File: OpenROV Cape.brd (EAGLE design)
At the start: 71.8 x 54.6 mm, 22 parts, among them IC1 ATMEGA328P-PU, T2 TIP122, T3 2N2222

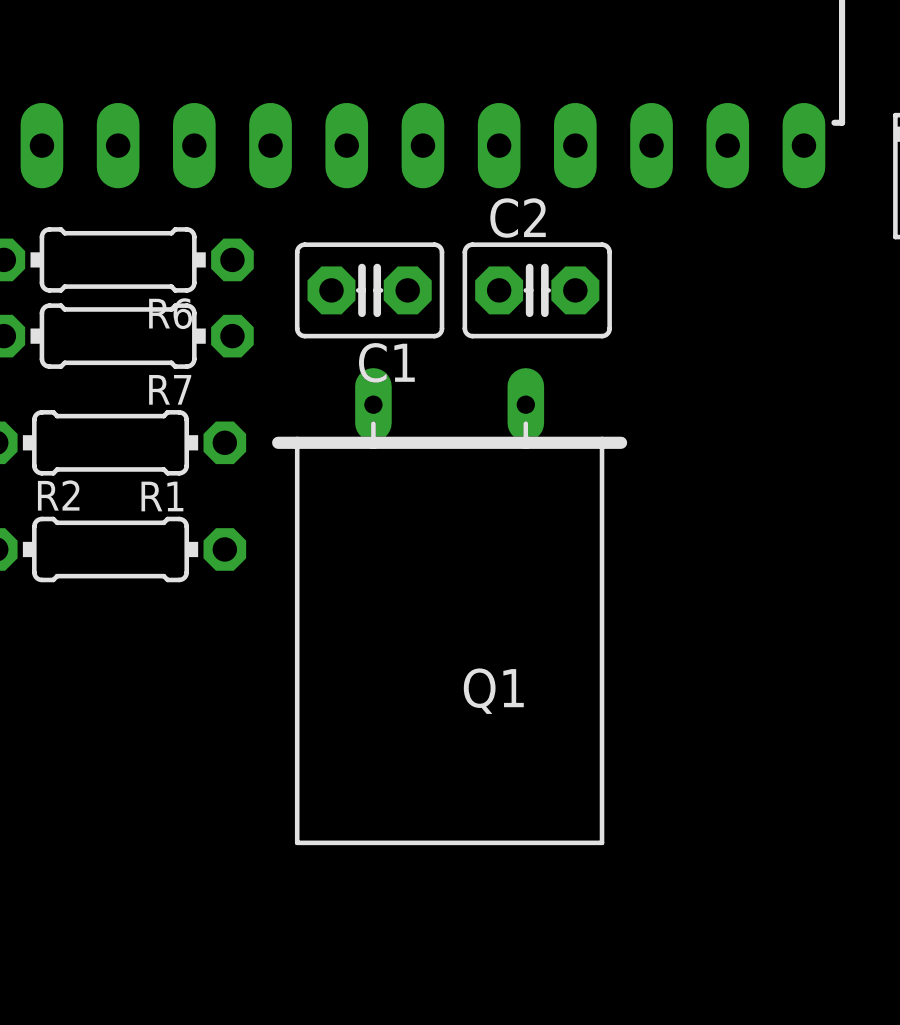
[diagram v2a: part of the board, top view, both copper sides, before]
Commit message: swapped out the giant crystal footprint for a smaller standard one with the same hole spacing
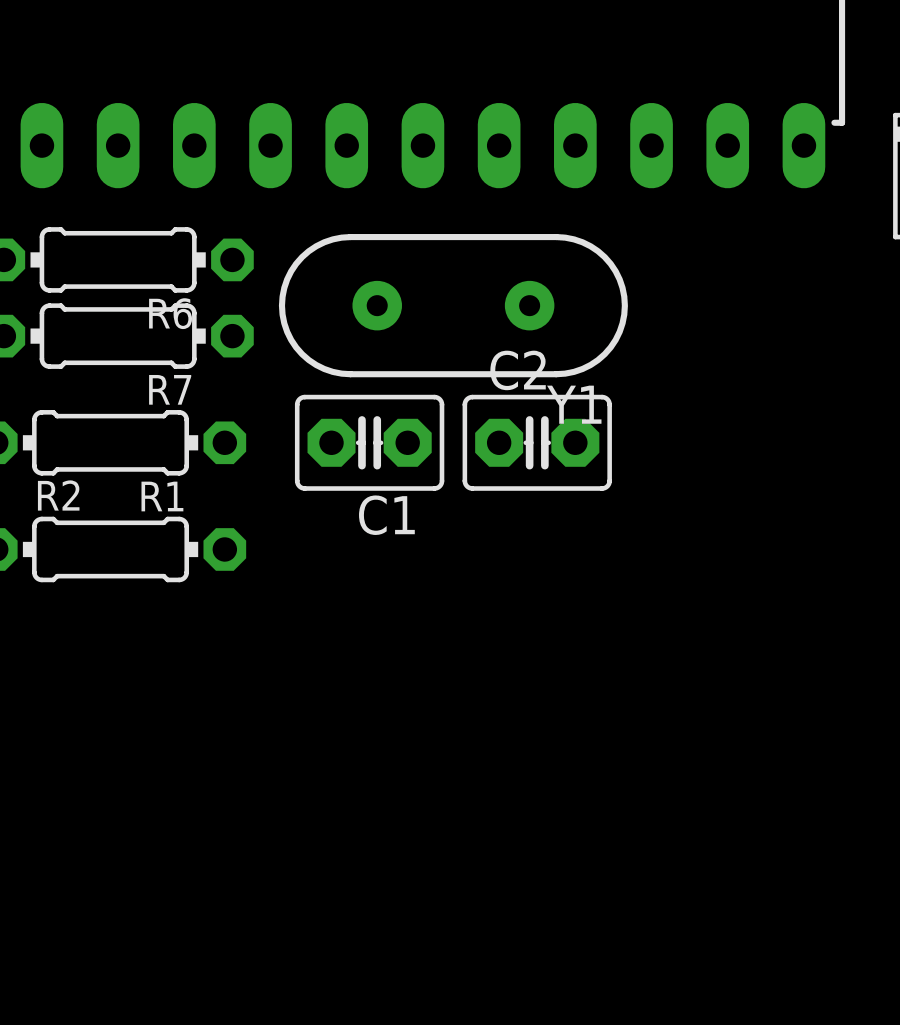
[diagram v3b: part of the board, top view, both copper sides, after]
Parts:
- removed Q1: (no value), special:Q
- added Y1: 16Mhz, SparkFun:HC49US
- moved C1 5.08 mm to (45.2, 25.7)
- moved C2 5.08 mm to (50.8, 25.7)
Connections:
- net N$24: now also Y1.1; no longer Q1.1
- net N$25: now also Y1.2; no longer Q1.2
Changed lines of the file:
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@@
 <element name="R1" library="rcl" package="0204/7" value="" x="36.576" y="25.654" rot="R180"/>
 <element name="R2" library="rcl" package="0204/7" value="" x="36.576" y="22.098"/>
-<element name="Q1" library="special" package="Q" value="" x="47.879" y="19.304" rot="R180"/>
-<element name="C1" library="capacitor-wima" package="C2.5-3" value="" x="45.212" y="30.734" rot="R180"/>
-<element name="C2" library="capacitor-wima" package="C2.5-3" value="" x="50.8" y="30.734"/>
+<element name="C1" library="capacitor-wima" package="C2.5-3" value="" x="45.212" y="25.654" rot="R180"/>
+<element name="C2" library="capacitor-wima" package="C2.5-3" value="" x="50.8" y="25.654"/>
 <element name="D1" library="diode" package="DO41-10" value="1N4004" x="66.548" y="34.544" rot="R270"/>
 <element name="D2" library="diode" package="DO41-10" value="1N4004" x="69.85" y="22.352" rot="R90"/>
@@
 <element name="T3" library="transistor" package="TO18" value="2N2222" x="29.21" y="27.94" rot="R90"/>
 <element name="R7" library="rcl" package="0204/7" value="" x="36.83" y="29.21" rot="R180"/>
+<element name="Y1" library="SparkFun" package="HC49US" value="16Mhz" x="48.006" y="30.226" rot="R180"/>
 </elements>
 <signals>
@@
 <contactref element="T3" pad="1"/>
 <wire x1="66.802" y1="23.368" x2="75.438" y2="24.892" width="0" layer="19" extent="1-1"/>
-<wire x1="52.07" y1="30.734" x2="66.802" y2="23.368" width="0" layer="19" extent="1-1"/>
+<wire x1="52.07" y1="25.654" x2="66.802" y2="23.368" width="0" layer="19" extent="1-1"/>
 <wire x1="72.39" y1="4.445" x2="66.802" y2="23.368" width="0" layer="19" extent="1-1"/>
-<wire x1="40.386" y1="25.654" x2="52.07" y2="30.734" width="0" layer="19" extent="1-1"/>
-<wire x1="43.942" y1="30.734" x2="40.386" y2="25.654" width="0" layer="19" extent="1-1"/>
+<wire x1="40.386" y1="25.654" x2="52.07" y2="25.654" width="0" layer="19" extent="1-1"/>
+<wire x1="43.942" y1="25.654" x2="40.386" y2="25.654" width="0" layer="19" extent="1-1"/>
 <wire x1="22.352" y1="19.558" x2="40.386" y2="25.654" width="0" layer="19" extent="1-1"/>
 <wire x1="22.352" y1="29.464" x2="22.352" y2="19.558" width="0" layer="19" extent="1-1"/>
@@
 </signal>
 <signal name="N$24">
-<contactref element="Q1" pad="1"/>
 <contactref element="C2" pad="1"/>
 <contactref element="IC1" pad="10"/>
-<wire x1="49.53" y1="30.734" x2="49.53" y2="35.56" width="0" layer="19" extent="1-1"/>
-<wire x1="50.419" y1="26.924" x2="49.53" y2="30.734" width="0" layer="19" extent="1-1"/>
+<contactref element="Y1" pad="1"/>
+<wire x1="49.53" y1="25.654" x2="49.53" y2="35.56" width="0" layer="19" extent="1-1"/>
+<wire x1="50.546" y1="30.226" x2="49.53" y2="25.654" width="0" layer="19" extent="1-1"/>
 </signal>
 <signal name="N$25">
-<contactref element="Q1" pad="2"/>
 <contactref element="C1" pad="1"/>
 <contactref element="IC1" pad="9"/>
-<wire x1="46.482" y1="30.734" x2="46.99" y2="35.56" width="0" layer="19" extent="1-1"/>
-<wire x1="45.339" y1="26.924" x2="46.482" y2="30.734" width="0" layer="19" extent="1-1"/>
+<contactref element="Y1" pad="2"/>
+<wire x1="46.482" y1="25.654" x2="46.99" y2="35.56" width="0" layer="19" extent="1-1"/>
+<wire x1="45.466" y1="30.226" x2="46.482" y2="25.654" width="0" layer="19" extent="1-1"/>
 </signal>
 <signal name="N$71">

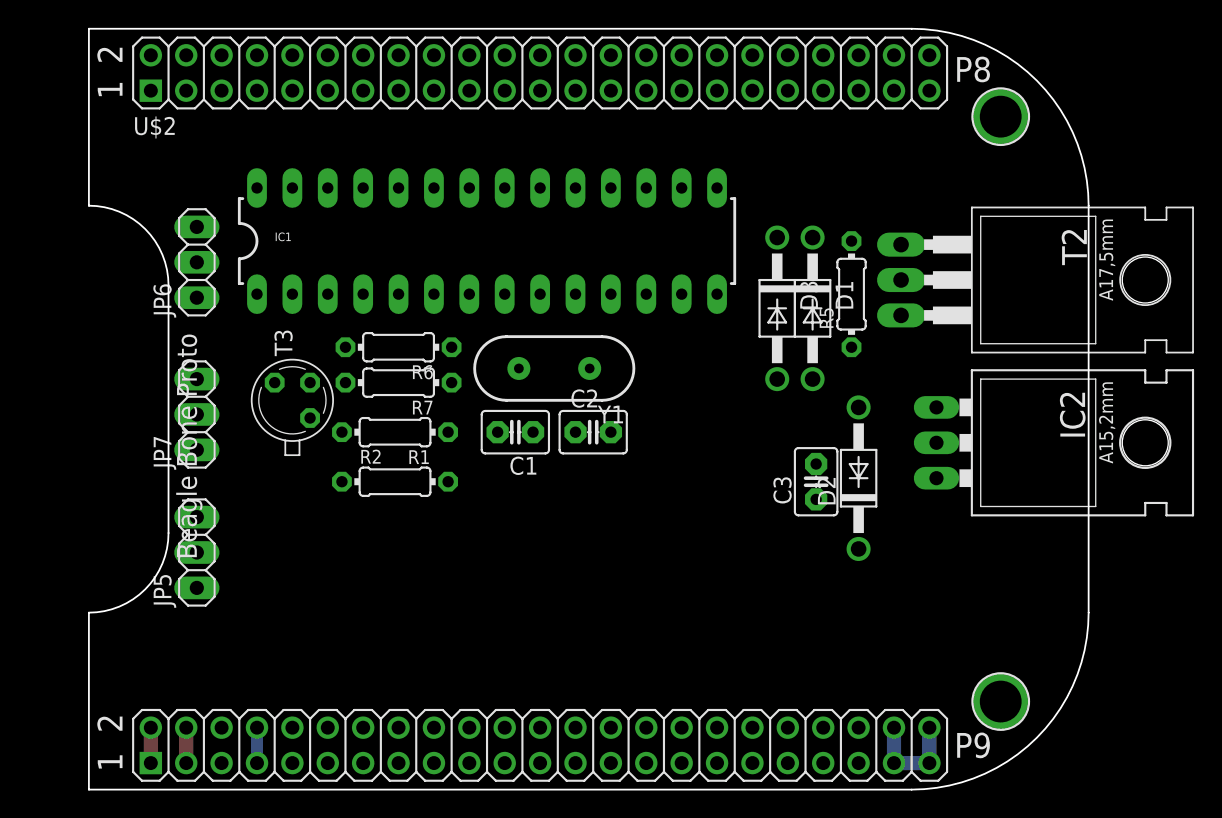
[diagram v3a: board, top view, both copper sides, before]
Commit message: moved servo headers back over to the right side of the board
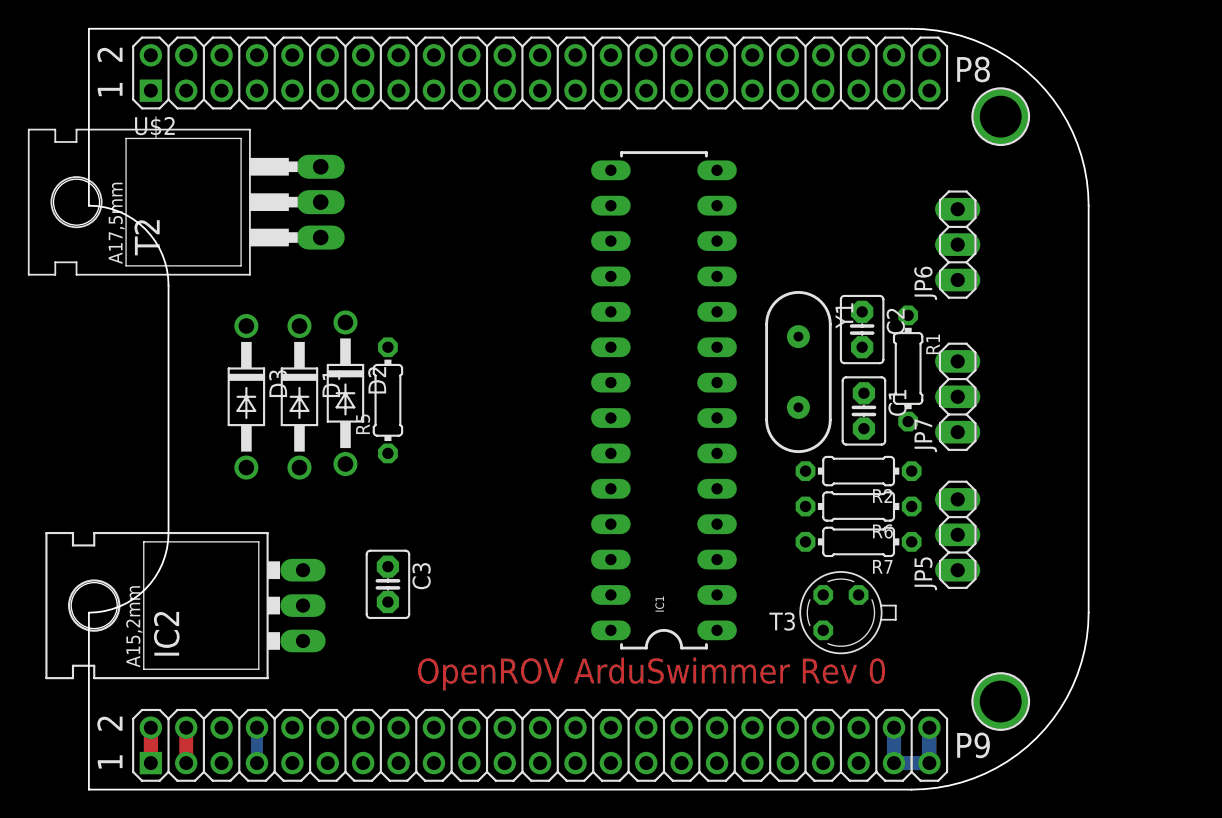
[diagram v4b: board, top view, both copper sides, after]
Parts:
- moved T2 54.6 mm to (24.9, 42.2), turned to 90 degrees
- moved JP5 54.6 mm to (77.0, 18.3)
- moved JP6 54.6 mm to (77.0, 39.1)
- moved JP7 54.6 mm to (77.0, 28.2)
- moved IC2 54.4 mm to (26.2, 13.2), turned to 90 degrees
- moved T3 42.2 mm to (68.6, 12.7), turned to 180 degrees
- moved D3 38.6 mm to (25.9, 28.2)
- moved D1 37.4 mm to (29.7, 28.2)
- moved D2 37.3 mm to (33.0, 28.4), turned to 270 degrees
- moved R1 37.1 mm to (73.4, 30.2), turned to 270 degrees
- moved R6 34.9 mm to (69.8, 20.3)
- moved R7 34.9 mm to (69.8, 17.8)
- moved R5 34.1 mm to (36.1, 27.9)
- moved R2 33.3 mm to (69.8, 22.9), turned to 180 degrees
- moved C3 31.6 mm to (36.1, 14.7), turned to 270 degrees
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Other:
- board text added: "OpenROV ArduSwimmer Rev 0"
- board text removed: "Beagle Bone Proto"

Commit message: added headers for +9V and +12V
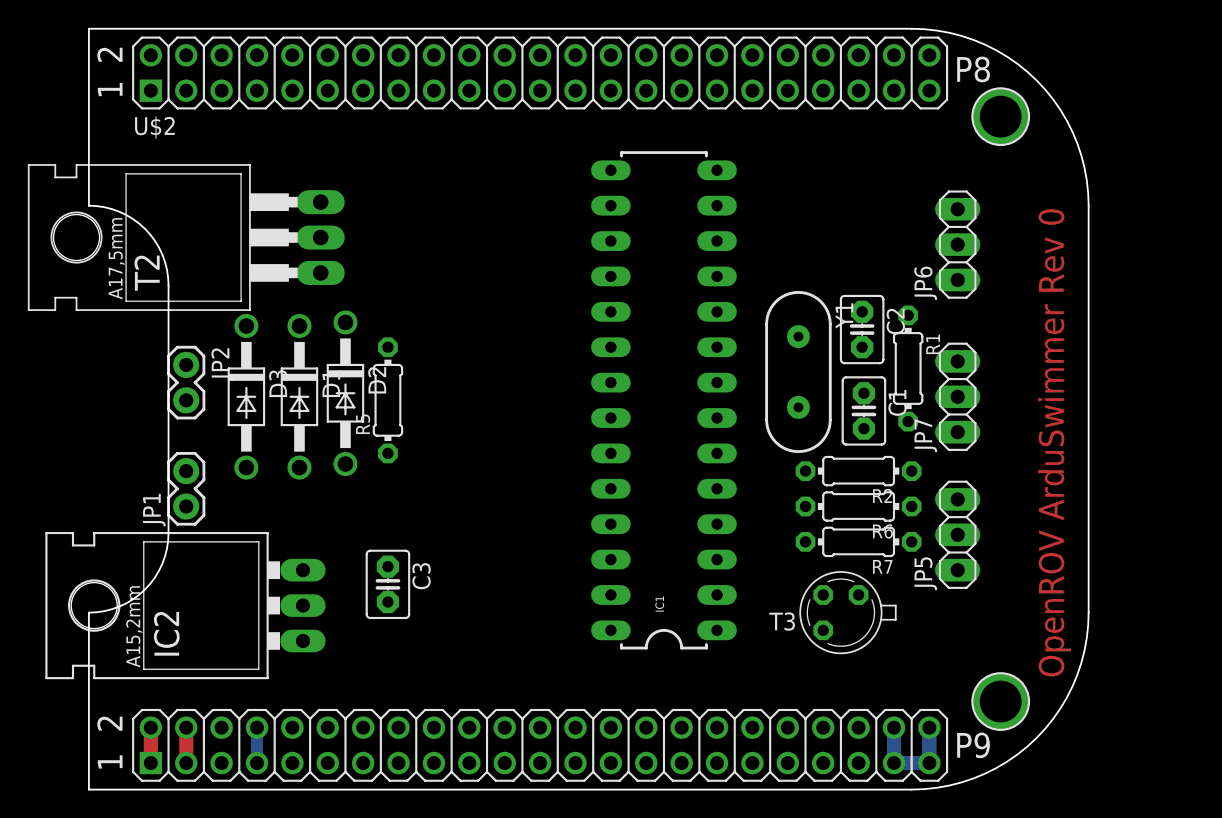
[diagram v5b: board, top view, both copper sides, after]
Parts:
- added JP1, JP2: (no value), SparkFun:1X02
- moved T2 2.54 mm to (24.9, 39.6)
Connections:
- net +12V: now also JP2.2
- net +9V: now also JP1.2
- net GND: now also JP1.1, JP2.1
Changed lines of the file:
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@@
 <text x="76.708" y="2.286" size="1.778" layer="21">P9</text>
 <text x="76.708" y="50.8" size="1.778" layer="21">P8</text>
-<text x="38.1" y="7.62" size="1.778" layer="1">OpenROV ArduSwimmer Rev 0</text>
+<text x="84.582" y="8.001" size="1.778" layer="1" rot="R90">OpenROV ArduSwimmer Rev 0</text>
 </plain>
 <attributes>
@@
 <element name="D2" library="diode" package="DO41-10" value="1N4004" x="33.02" y="28.448" rot="R270"/>
 <element name="R5" library="rcl" package="0204/7" value="" x="36.068" y="27.94" rot="R90"/>
-<element name="T2" library="transistor" package="TO220" value="TIP122" x="24.892" y="42.164" rot="R90"/>
+<element name="T2" library="transistor" package="TO220" value="TIP122" x="24.892" y="39.624" rot="R90"/>
 <element name="C3" library="capacitor-wima" package="C2.5-3" value="" x="36.068" y="14.732" rot="R270"/>
 <element name="D3" library="diode" package="DO41-10" value="1N4004" x="25.908" y="28.194" rot="R270"/>
@@
 <element name="R7" library="rcl" package="0204/7" value="" x="69.85" y="17.78" rot="R180"/>
 <element name="Y1" library="SparkFun" package="HC49US" value="16Mhz" x="65.532" y="29.972" rot="R270"/>
+<element name="JP1" library="SparkFun" package="1X02" value="" x="21.59" y="20.32" rot="R90"/>
+<element name="JP2" library="SparkFun" package="1X02" value="" x="21.59" y="30.48" rot="R270"/>
 </elements>
 <signals>
@@
 <contactref element="U$2" pad="1"/>
 <contactref element="T3" pad="1"/>
-<wire x1="36.068" y1="13.462" x2="29.972" y2="13.208" width="0" layer="19" extent="1-1"/>
-<wire x1="70.104" y1="31.75" x2="36.068" y2="13.462" width="0" layer="19" extent="1-1"/>
-<wire x1="72.39" y1="4.445" x2="36.068" y2="13.462" width="0" layer="19" extent="1-1"/>
-<wire x1="73.406" y1="34.036" x2="70.104" y2="31.75" width="0" layer="19" extent="1-1"/>
-<wire x1="70.231" y1="25.908" x2="73.406" y2="34.036" width="0" layer="19" extent="1-1"/>
-<wire x1="76.962" y1="20.828" x2="73.406" y2="34.036" width="0" layer="19" extent="1-1"/>
-<wire x1="76.962" y1="30.734" x2="76.962" y2="20.828" width="0" layer="19" extent="1-1"/>
-<wire x1="76.962" y1="41.656" x2="76.962" y2="30.734" width="0" layer="19" extent="1-1"/>
-<wire x1="19.05" y1="50.165" x2="76.962" y2="41.656" width="0" layer="19" extent="1-1"/>
+<contactref element="JP2" pad="1"/>
+<contactref element="JP1" pad="1"/>
+<wire x1="73.406" y1="34.036" x2="76.962" y2="41.656" width="0" layer="19" extent="1-1"/>
+<wire x1="70.104" y1="31.75" x2="73.406" y2="34.036" width="0" layer="19" extent="1-1"/>
+<wire x1="76.962" y1="30.734" x2="73.406" y2="34.036" width="0" layer="19" extent="1-1"/>
+<wire x1="70.231" y1="25.908" x2="70.104" y2="31.75" width="0" layer="19" extent="1-1"/>
+<wire x1="76.962" y1="20.828" x2="70.231" y2="25.908" width="0" layer="19" extent="1-1"/>
+<wire x1="69.85" y1="13.97" x2="76.962" y2="20.828" width="0" layer="19" extent="1-1"/>
+<wire x1="72.39" y1="4.445" x2="69.85" y2="13.97" width="0" layer="19" extent="1-1"/>
+<wire x1="36.068" y1="13.462" x2="69.85" y2="13.97" width="0" layer="19" extent="1-1"/>
+<wire x1="29.972" y1="13.208" x2="36.068" y2="13.462" width="0" layer="19" extent="1-1"/>
+<wire x1="19.05" y1="4.445" x2="29.972" y2="13.208" width="0" layer="19" extent="1-1"/>
+<wire x1="21.59" y1="20.32" x2="19.05" y2="1.905" width="0" layer="19" extent="1-1"/>
+<wire x1="21.59" y1="30.48" x2="21.59" y2="20.32" width="0" layer="19" extent="1-1"/>
+<wire x1="19.05" y1="50.165" x2="29.972" y2="13.208" width="0" layer="19" extent="1-1"/>
 <wire x1="19.05" y1="52.705" x2="19.05" y2="50.165" width="0" layer="19" extent="1-1"/>
-<wire x1="19.05" y1="4.445" x2="76.962" y2="20.828" width="0" layer="19" extent="1-1"/>
-<wire x1="69.85" y1="13.97" x2="19.05" y2="1.905" width="0" layer="19" extent="1-1"/>
 </signal>
 <signal name="N$24">
@@
 <contactref element="T2" pad="1"/>
 <contactref element="R5" pad="2"/>
-<wire x1="36.068" y1="31.75" x2="31.242" y2="39.624" width="0" layer="19" extent="1-1"/>
+<wire x1="36.068" y1="31.75" x2="31.242" y2="37.084" width="0" layer="19" extent="1-1"/>
 </signal>
 <signal name="N$90">
@@
 <contactref element="D3" pad="C"/>
 <contactref element="T2" pad="2"/>
-<wire x1="29.718" y1="33.274" x2="31.242" y2="42.164" width="0" layer="19" extent="1-1"/>
+<wire x1="29.718" y1="33.274" x2="31.242" y2="39.624" width="0" layer="19" extent="1-1"/>
 <wire x1="25.908" y1="33.274" x2="29.718" y2="33.274" width="0" layer="19" extent="1-1"/>
 </signal>
@@
 <contactref element="IC2" pad="IN"/>
 <contactref element="T2" pad="3"/>
-<wire x1="29.972" y1="10.668" x2="31.242" y2="44.704" width="0" layer="19" extent="1-1"/>
+<wire x1="29.972" y1="10.668" x2="31.242" y2="42.164" width="0" layer="19" extent="1-1"/>
 </signal>
 <signal name="+9V">
 <contactref element="D3" pad="A"/>
+<contactref element="JP1" pad="2"/>
+<wire x1="21.59" y1="22.86" x2="25.908" y2="23.114" width="0" layer="19" extent="1-1"/>
 </signal>
 <signal name="+12V">
 <contactref element="D2" pad="A"/>
 <contactref element="D1" pad="A"/>
+<contactref element="JP2" pad="2"/>
 <wire x1="29.718" y1="23.114" x2="33.02" y2="23.368" width="0" layer="19" extent="1-1"/>
+<wire x1="21.59" y1="27.94" x2="29.718" y2="23.114" width="0" layer="19" extent="1-1"/>
 </signal>
 <signal name="VCC">
